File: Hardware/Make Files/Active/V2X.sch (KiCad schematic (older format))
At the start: 0 parts

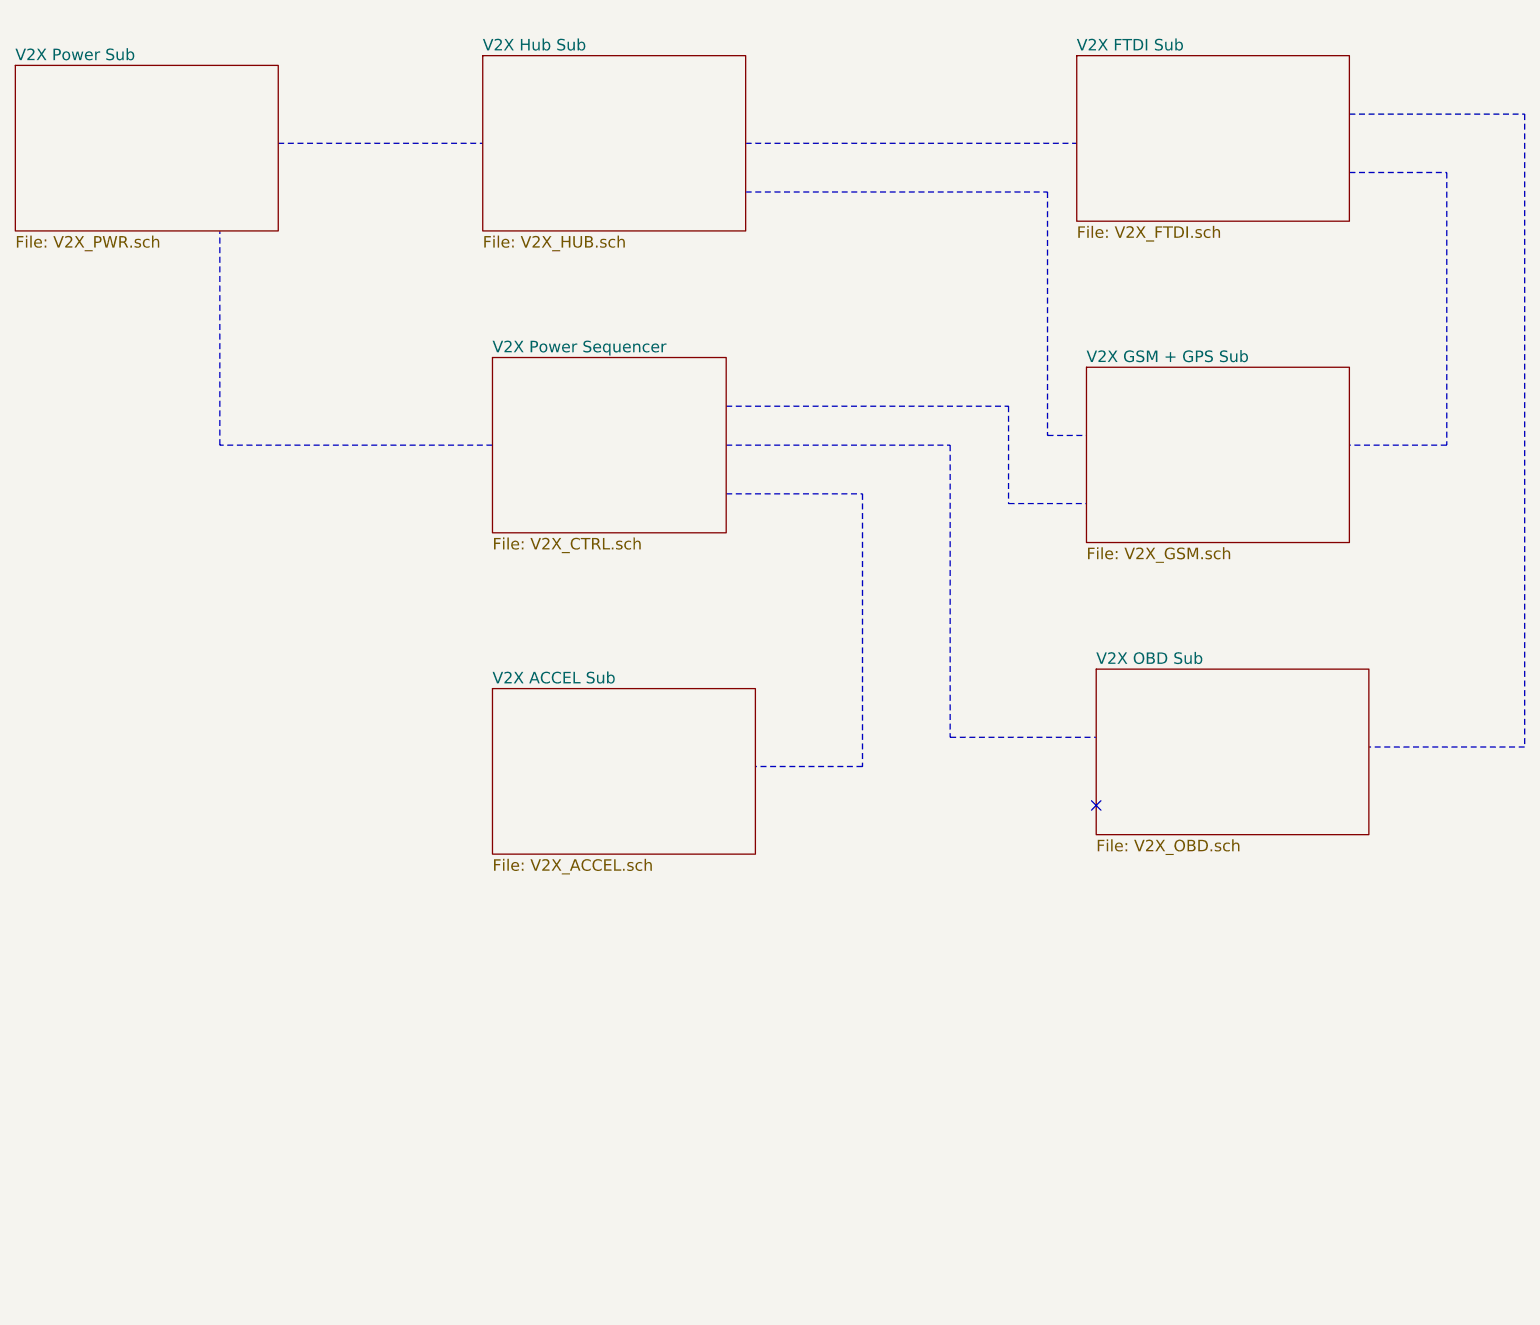
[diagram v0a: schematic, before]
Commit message: Saving V1.1 as archive.
We are trying a new architecture where the FTDI can be removed. making a
backup spot
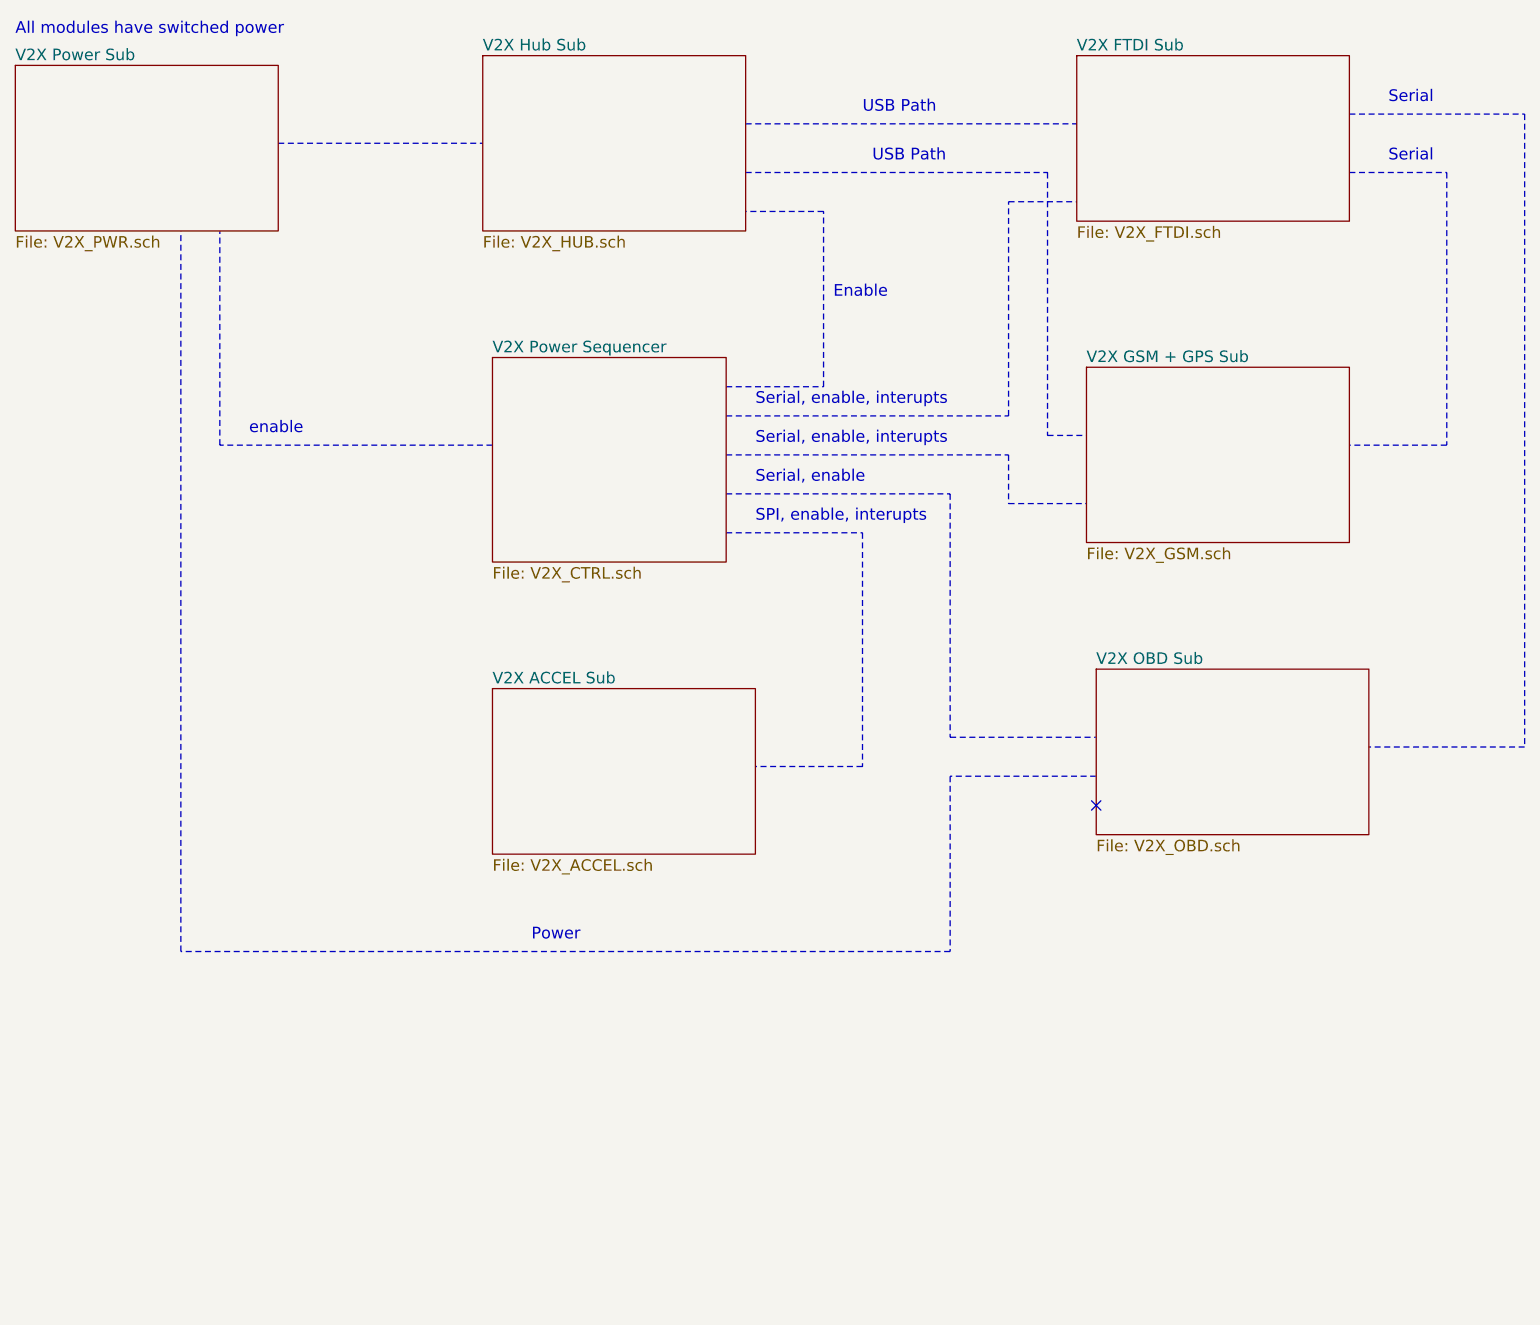
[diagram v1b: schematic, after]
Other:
- note added: "All modules have switched power"
- note added: "Enable"
- note added: "Power"
- note added: "SPI, enable, interupts"
- note added: "Serial"
- note added: "Serial, enable"
- note added: "Serial, enable, interupts"
- note added: "USB Path"
- note added: "enable"
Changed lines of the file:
@@
 $EndSheet
 $Sheet
-S 4400 2650 1200 900
+S 4400 2650 1200 1050
 U 55F91B74
 F0 "V2X Power Sequencer" 59
@@
 	3300 1550 4350 1550
 Wire Notes Line
-	5700 1550 7400 1550
+	5700 1450 7400 1450
 Wire Notes Line
 	8800 1700 9300 1700
@@
 	9700 4650 8900 4650
 Wire Notes Line
-	5600 3100 6750 3100
+	5600 3350 6750 3350
 Wire Notes Line
-	6750 3100 6750 4600
+	6750 3350 6750 4600
 Wire Notes Line
 	6750 4600 7500 4600
 Wire Notes Line
-	5600 3350 6300 3350
+	5600 3550 6300 3550
 Wire Notes Line
-	6300 3350 6300 4750
+	6300 3550 6300 4750
 Wire Notes Line
 	6300 4750 5750 4750
 Wire Notes Line
-	5600 2900 7050 2900
+	5600 3150 7050 3150
 Wire Notes Line
-	7050 2900 7050 3400
+	7050 3150 7050 3400
 Wire Notes Line
 	7050 3400 7450 3400
 Wire Notes Line
-	5700 1800 7250 1800
+	5700 1700 7250 1700
 Wire Notes Line
-	7250 1800 7250 3050
+	7250 1700 7250 3050
 Wire Notes Line
 	7250 3050 7450 3050
+Wire Notes Line
+	5600 2800 6100 2800
+Wire Notes Line
+	6100 2800 6100 1900
+Wire Notes Line
+	6100 1900 5700 1900
+Text Notes 6150 2350 0    60   ~ 0
+Enable
+Text Notes 6300 1400 0    60   ~ 0
+USB Path
+Text Notes 6350 1650 0    60   ~ 0
+USB Path
+Text Notes 9000 1350 0    60   ~ 0
+Serial
+Text Notes 9000 1650 0    60   ~ 0
+Serial
+Text Notes 5750 3100 0    60   ~ 0
+Serial, enable, interupts
+Text Notes 5750 3300 0    60   ~ 0
+Serial, enable
+Text Notes 5750 3500 0    60   ~ 0
+SPI, enable, interupts
+Text Notes 3150 3050 0    60   ~ 0
+enable
+Text Notes 1950 1000 0    60   ~ 0
+All modules have switched power
+Wire Notes Line
+	7500 4800 6750 4800
+Wire Notes Line
+	6750 4800 6750 5700
+Wire Notes Line
+	6750 5700 2800 5700
+Wire Notes Line
+	2800 5700 2800 2000
+Text Notes 4600 5650 0    60   ~ 0
+Power
+Text Notes 5750 2900 0    60   ~ 0
+Serial, enable, interupts
+Wire Notes Line
+	5600 2950 7050 2950
+Wire Notes Line
+	7050 2950 7050 1850
+Wire Notes Line
+	7050 1850 7400 1850
 $EndSCHEMATC

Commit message: Project rework
Split the Main and GSM boards into separate projects, redesigned Main
board after flaws were found.
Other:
- note added: "GSM GPS Sheet\nMoved to seperate\nKicad project"
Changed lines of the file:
@@
 $Descr USLetter 11000 8500
 encoding utf-8
-Sheet 1 8
+Sheet 1 7
 Title "V2X - Open source RVI over SMS daughter card"
 Date "2015-07-17"
@@
 F0 "V2X FTDI Sub" 59
 F1 "V2X_FTDI.sch" 59
-$EndSheet
-$Sheet
-S 7450 2700 1350 900
-U 55AF97E0
-F0 "V2X GSM + GPS Sub" 59
-F1 "V2X_GSM.sch" 59
 $EndSheet
 NoConn ~ 7500 4950
@@
 Wire Notes Line
 	7050 1850 7400 1850
+Wire Notes Line
+	7450 2700 7450 3700
+Wire Notes Line
+	7450 3700 8800 3700
+Wire Notes Line
+	8800 3700 8800 2700
+Wire Notes Line
+	8800 2700 7450 2700
+Text Notes 7600 3300 0    69   ~ 0
+GSM GPS Sheet\nMoved to seperate\nKicad project
 $EndSCHEMATC

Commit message: Added USB-A to design
discovered the Rpi cannot be back fed over USB, had to add a power Port
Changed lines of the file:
@@
 $Descr USLetter 11000 8500
 encoding utf-8
-Sheet 1 7
+Sheet 1 8
 Title "V2X - Open source RVI over SMS daughter card"
 Date "2015-07-17"
@@
 Text Notes 7600 3300 0    69   ~ 0
 GSM GPS Sheet\nMoved to seperate\nKicad project
+$Sheet
+S 3750 6600 1350 800
+U 562004BB
+F0 "Sheet562004BA" 69
+F1 "V2X_GSM.sch" 69
+$EndSheet
 $EndSCHEMATC

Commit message: work from home day
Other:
- note added: "2x Serial, enable"
- note added: "Enable, \nSMB config,\nUSB"
- note added: "GSM GPS Sheet\nMoved to seperate\nKicad project and \nseperate PCB"
- note added: "USB"
- note removed: "Enable"
- note removed: "GSM GPS Sheet\nMoved to seperate\nKicad project"
- note removed: "USB Path"
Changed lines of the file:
@@
 	6100 1900 5700 1900
 Text Notes 6150 2350 0    60   ~ 0
-Enable
+Enable, \nSMB config,\nUSB
 Text Notes 6300 1400 0    60   ~ 0
-USB Path
+USB
 Text Notes 6350 1650 0    60   ~ 0
-USB Path
+USB
 Text Notes 9000 1350 0    60   ~ 0
 Serial
@@
 Power
 Text Notes 5750 2900 0    60   ~ 0
-Serial, enable, interupts
+2x Serial, enable
 Wire Notes Line
 	5600 2950 7050 2950
@@
 Wire Notes Line
 	8800 3700 8800 2700
+Text Notes 7600 3300 0    69   ~ 0
+GSM GPS Sheet\nMoved to seperate\nKicad project and \nseperate PCB
+$Sheet
+S 7450 2700 1350 1000
+U 562004BB
+F0 "GSM+GPS" 69
+F1 "V2X_GSM.sch" 69
+$EndSheet
 Wire Notes Line
 	8800 2700 7450 2700
-Text Notes 7600 3300 0    69   ~ 0
-GSM GPS Sheet\nMoved to seperate\nKicad project
-$Sheet
-S 3750 6600 1350 800
-U 562004BB
-F0 "Sheet562004BA" 69
-F1 "V2X_GSM.sch" 69
-$EndSheet
 $EndSCHEMATC

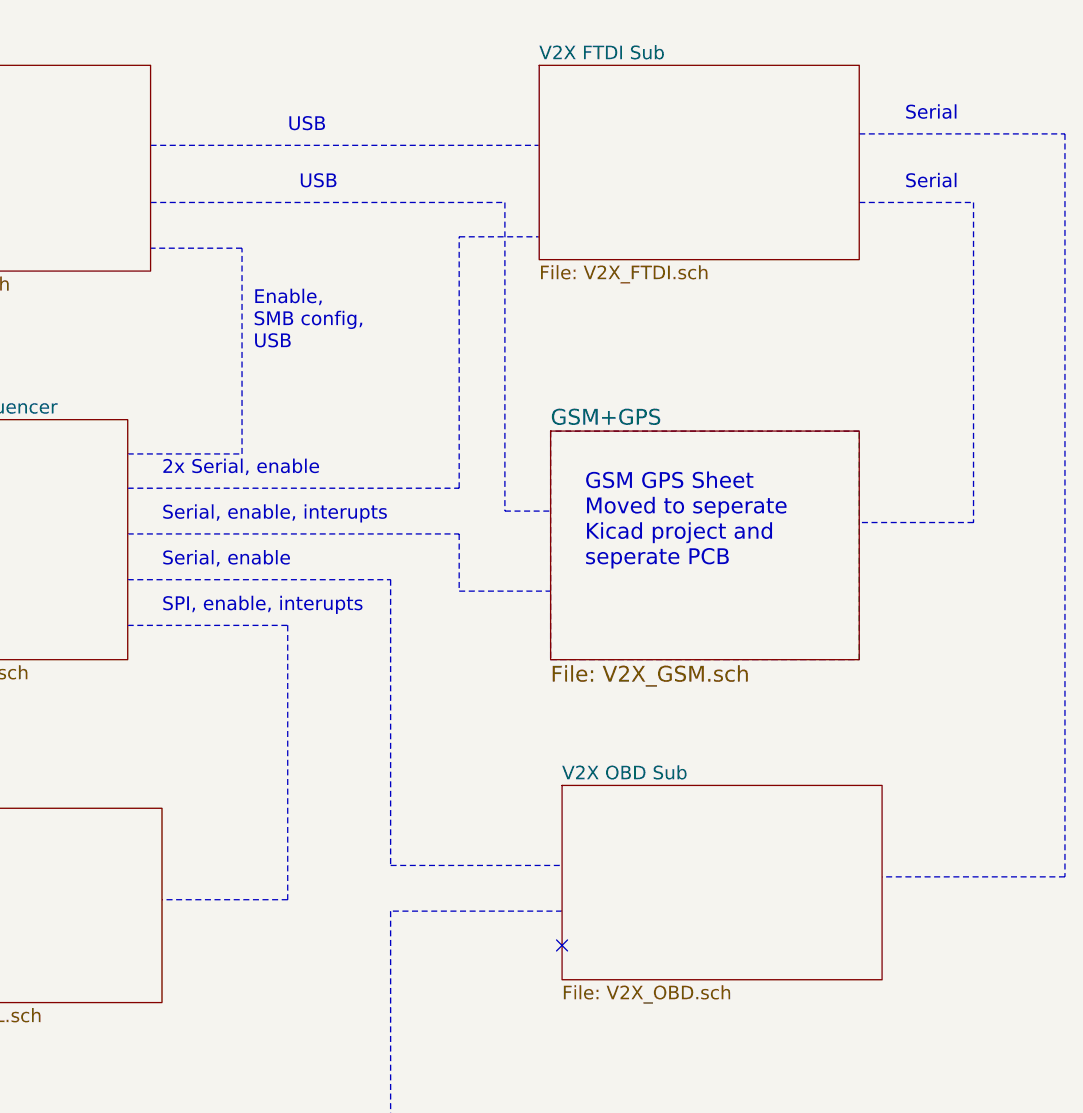
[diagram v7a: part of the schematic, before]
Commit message: Verification findings and modifications
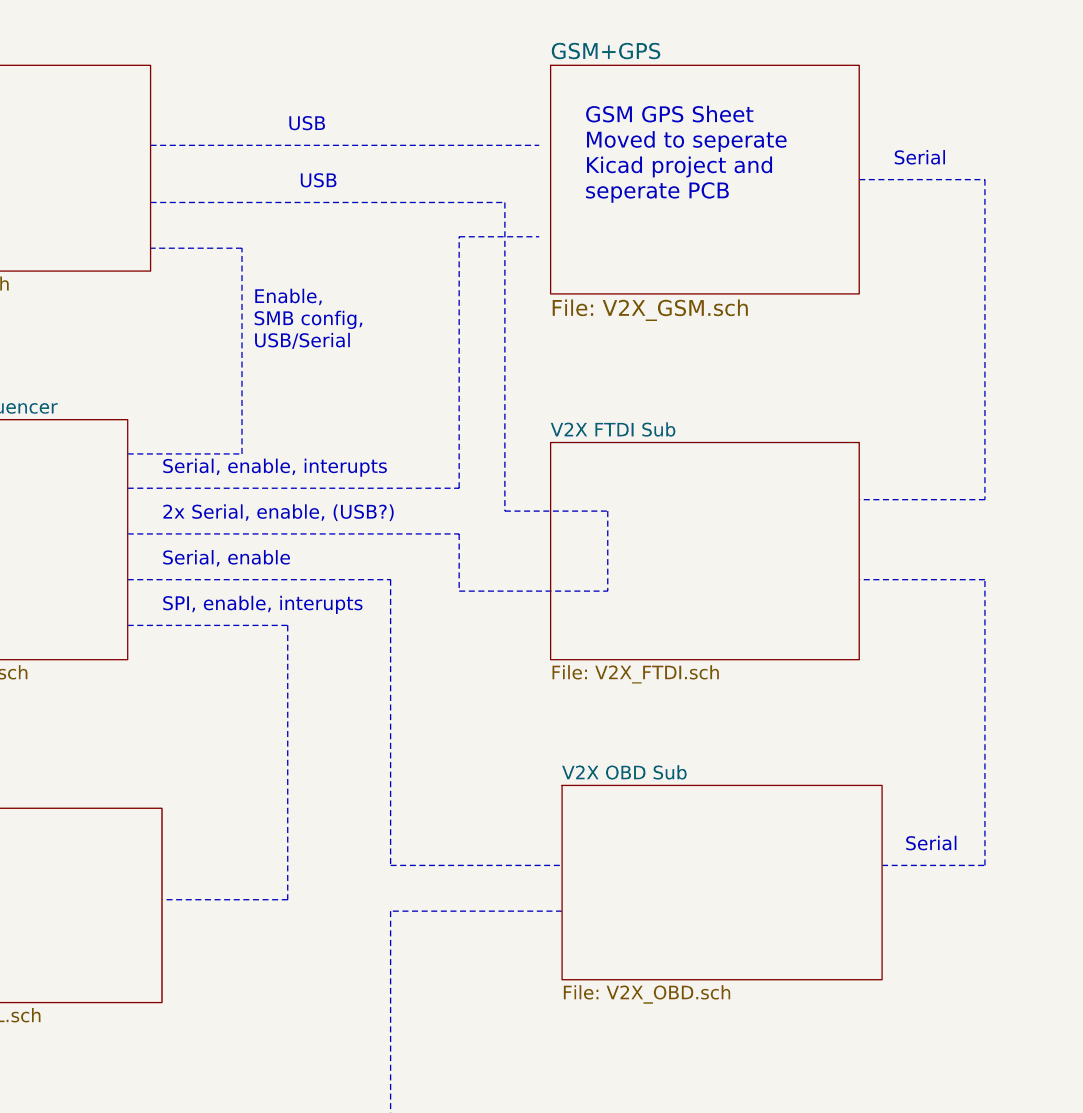
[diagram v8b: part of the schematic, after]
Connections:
- no-connect marks 1 -> 0
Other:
- note added: "2x Serial, enable, (USB?)"
- note added: "Enable, \nSMB config,\nUSB/Serial"
- note removed: "2x Serial, enable"
- note removed: "Enable, \nSMB config,\nUSB"
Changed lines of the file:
@@
 $EndDescr
 $Sheet
-S 7400 1100 1400 850
+S 7450 2750 1350 950
 U 55AB1D0F
 F0 "V2X FTDI Sub" 59
 F1 "V2X_FTDI.sch" 59
 $EndSheet
-NoConn ~ 7500 4950
 $Sheet
 S 7500 4250 1400 850
@@
 	5700 1450 7400 1450
 Wire Notes Line
-	8800 1700 9300 1700
-Wire Notes Line
-	9300 1700 9300 3100
-Wire Notes Line
-	9300 3100 8800 3100
-Wire Notes Line
-	8800 1400 9700 1400
-Wire Notes Line
-	9700 1400 9700 4650
-Wire Notes Line
-	9700 4650 8900 4650
-Wire Notes Line
 	5600 3350 6750 3350
 Wire Notes Line
@@
 	7050 3150 7050 3400
 Wire Notes Line
-	7050 3400 7450 3400
+	7050 3400 7700 3400
 Wire Notes Line
 	5700 1700 7250 1700
@@
 	7250 1700 7250 3050
 Wire Notes Line
-	7250 3050 7450 3050
+	7250 3050 7700 3050
 Wire Notes Line
 	5600 2800 6100 2800
@@
 	6100 1900 5700 1900
 Text Notes 6150 2350 0    60   ~ 0
-Enable, \nSMB config,\nUSB
+Enable, \nSMB config,\nUSB/Serial
 Text Notes 6300 1400 0    60   ~ 0
 USB
 Text Notes 6350 1650 0    60   ~ 0
 USB
-Text Notes 9000 1350 0    60   ~ 0
+Text Notes 8950 1550 0    60   ~ 0
 Serial
-Text Notes 9000 1650 0    60   ~ 0
+Text Notes 9000 4550 0    60   ~ 0
 Serial
-Text Notes 5750 3100 0    60   ~ 0
+Text Notes 5750 2900 0    60   ~ 0
 Serial, enable, interupts
 Text Notes 5750 3300 0    60   ~ 0
@@
 Text Notes 4600 5650 0    60   ~ 0
 Power
-Text Notes 5750 2900 0    60   ~ 0
-2x Serial, enable
+Text Notes 5750 3100 0    60   ~ 0
+2x Serial, enable, (USB?)
 Wire Notes Line
 	5600 2950 7050 2950
@@
 Wire Notes Line
 	7050 1850 7400 1850
+Text Notes 7600 1700 0    69   ~ 0
+GSM GPS Sheet\nMoved to seperate\nKicad project and \nseperate PCB
 Wire Notes Line
-	7450 2700 7450 3700
+	7700 3050 7700 3400
 Wire Notes Line
-	7450 3700 8800 3700
+	8900 4600 9350 4600
 Wire Notes Line
-	8800 3700 8800 2700
-Text Notes 7600 3300 0    69   ~ 0
-GSM GPS Sheet\nMoved to seperate\nKicad project and \nseperate PCB
+	9350 4600 9350 3350
+Wire Notes Line
+	9350 3350 8800 3350
+Wire Notes Line
+	8800 1600 9350 1600
+Wire Notes Line
+	9350 1600 9350 3000
+Wire Notes Line
+	9350 3000 8800 3000
 $Sheet
-S 7450 2700 1350 1000
+S 7450 1100 1350 1000
 U 562004BB
 F0 "GSM+GPS" 69
 F1 "V2X_GSM.sch" 69
 $EndSheet
-Wire Notes Line
-	8800 2700 7450 2700
 $EndSCHEMATC
